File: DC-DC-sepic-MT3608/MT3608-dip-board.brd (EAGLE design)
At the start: 20 x 20.3 mm, 8 parts

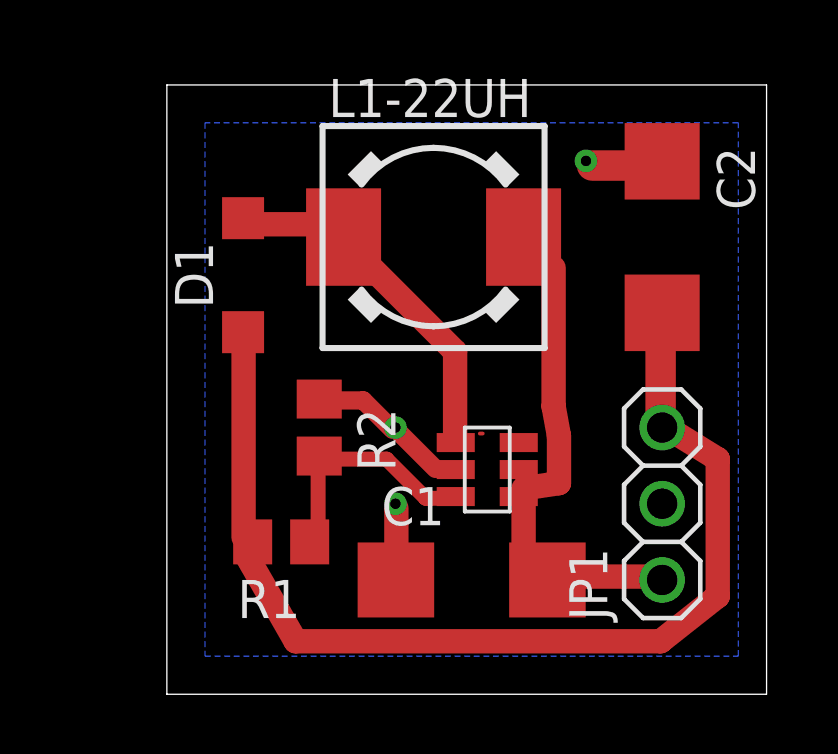
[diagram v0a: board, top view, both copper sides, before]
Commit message: DC-DC boards updated
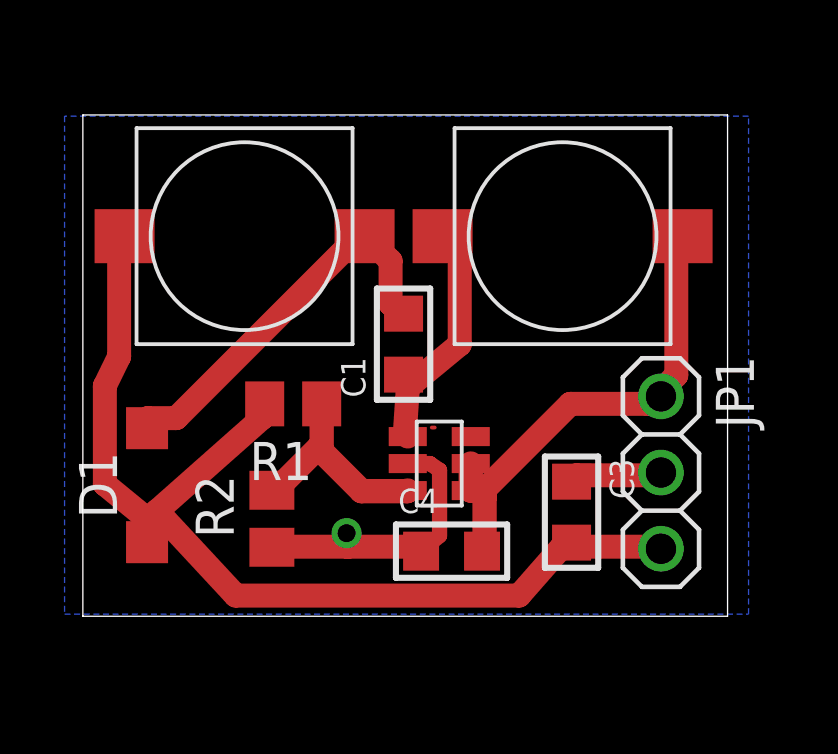
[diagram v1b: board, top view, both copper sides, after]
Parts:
- removed C2: 22uf, resistor:C/6032-28R
- removed L1-22UH: DR74, inductors:DR74
- added 22UH, U$3: CDRH74NP-220MC-B, mgvc:CDRH74NP-220MC-B
- added C3, C4: 28uf, rc-master-smd:C0805
- C1: value 22uf -> 5.6uf; device resistor:C/6032-28R -> rc-master-smd:C0805
- R2: value 15k -> 20k
- moved C1 8.18 mm to (37.1, 35.8), turned to 90 degrees
- moved D1 7.70 mm to (28.6, 31.1)
- moved R1 4.62 mm to (33.4, 33.8)
- moved R2 3.43 mm to (32.7, 30.0), turned to 90 degrees
- moved U$1 1.61 mm to (39.0, 33.2)
- moved JP1 1.04 mm to (45.7, 31.5), turned to 270 degrees
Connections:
- new net N$2: 22UH.P$2, C1.2, D1.A
- net GND: now also C3.1, C4.1; no longer C1.-, C2.-
- net N$1: now also C4.2, U$3.P$2; no longer C1.+, L1-22UH.2
- net N$3: now also C1.1, U$3.P$1; no longer D1.A, L1-22UH.1
- net N$4: now also 22UH.P$1, C3.2; no longer C2.+
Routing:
- net N$2: track 0.00 -> 13.4 mm
- net N$3: track 12.0 -> 8.29 mm
- net GND: track 10.8 -> 12.7 mm, vias 3 -> 1
- net N$1: track 18.0 -> 16.3 mm
- net N$5: track 8.18 -> 7.35 mm
- net N$4: track 36.4 -> 35.7 mm
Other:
- board size 20 x 20.3 mm -> 21.5 x 16.7 mm
